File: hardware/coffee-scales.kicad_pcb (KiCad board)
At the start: 2 copper layers, 121.9 x 50.8 mm, 34 parts, among them J2 Conn_01x05, J3 AVR-ISP-6, Q1 MMBT4403, SW1 SW_Push, SW2 SW_Push, U2 ATmega328P-A, U3 4DIGIT_7SEG, U4 4DIGIT_7SEG, Y1 8MHz

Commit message: Infinite schematic/PCB changes
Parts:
- removed C6: 10uF, Capacitor_SMD:C_1210_3225Metric
- removed C8: 10uF, Capacitor_SMD:C_0805_2012Metric
- removed REF** (x3): MountingHole_3.2mm_M3, MountingHole:MountingHole_3.2mm_M3
- removed U4: 4DIGIT_7SEG, CoffeeLib:4DIGIT_7SEG
- added C13: 100pF, Capacitor_SMD:C_0603_1608Metric, F.Cu at (125.1, 146.1)
- added C15: 100pF, Capacitor_SMD:C_0603_1608Metric, F.Cu at (74.3, 146.1)
- added C16: 100pF, Capacitor_SMD:C_0603_1608Metric, F.Cu at (74.3, 149.2)
- added C17: 100pF, Capacitor_SMD:C_0603_1608Metric, F.Cu at (125.1, 149.2)
- added C18: 0.1uF, Capacitor_SMD:C_0603_1608Metric, F.Cu at (120.0, 151.3)
- added C19: 0.1uF, Capacitor_SMD:C_0603_1608Metric, F.Cu at (69.2, 151.3)
- added R10: 10k, Resistor_SMD:R_0603_1608Metric, F.Cu at (123.2, 149.2)
- added R7: 10k, Resistor_SMD:R_0603_1608Metric, F.Cu at (123.2, 146.1)
- added R8: 10k, Resistor_SMD:R_0603_1608Metric, F.Cu at (72.4, 149.2)
- added R9: 10k, Resistor_SMD:R_0603_1608Metric, F.Cu at (72.4, 146.1)
- added U1: ~, Package_SO:SOP-20_7.5x12.8mm_P1.27mm, F.Cu at (62.2, 151.1)
- added U6: ~, CoffeeLib:7_segment, F.Cu at (119.4, 165.1)
- added U7: ~, CoffeeLib:7_segment, F.Cu at (68.6, 165.1)
- U3: value 4DIGIT_7SEG -> ~; footprint CoffeeLib:4DIGIT_7SEG -> Package_SO:SOP-20_7.5x12.8mm_P1.27mm
- moved U3 56.6 mm to (113.0, 151.1)
- moved R6 18.5 mm to (50.6, 141.6)
- moved D1 18.2 mm to (47.0, 141.6)
- moved C3 5.96 mm to (152.4, 134.6), turned to 0 degrees
- moved C7 5.90 mm to (151.8, 138.4), turned to 0 degrees
- moved R5 5.08 mm to (59.1, 131.3)
- moved SW2 4.45 mm to (54.8, 131.3)
- moved C11 3.81 mm to (50.8, 131.3)
- moved C10 3.29 mm to (69.2, 129.5), turned to 180 degrees
- moved C5 3.27 mm to (119.4, 137.3)
- moved SW1 1.27 mm to (87.7, 162.6)
- moved C12 1.17 mm to (126.2, 138.4), turned to 180 degrees
- moved C9 1.10 mm to (72.2, 127.6), turned to 180 degrees
- moved L1 0.21 mm to (135.3, 138.4)
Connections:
- C12 pad 1: +3V3 -> VCC
- C5 pad 1: +3V3 -> VCC
- Q1 pad 2: +3V3 -> VCC
- U3 pad 1: unconnected-(U3-CLK-Pad1) -> GND
- U3 pad 2: unconnected-(U3-DIO-Pad2) -> Net-(U3-SEG1)
- U3 pad 3: GND -> Net-(U3-SEG2)
- U3 pad 4: +3V3 -> Net-(U3-SEG3)
- U3 pad 5: /328P/GPIO2 -> Net-(U3-SEG4)
- U3 pad 6: /328P/GPIO1 -> Net-(U3-SEG5)
- U3 pad 7: GND -> Net-(U3-SEG6)
- U3 pad 8: unconnected-(U3-5V-Pad8) -> Net-(U3-SEG7)
- U5 pad 1: +3V3 -> VCC
- U5 pad 16: +3V3 -> VCC
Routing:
- net VCC: track 69.5 -> 216.9 mm, vias 2 -> 8
- net +3V3: track 132.9 -> 0.00 mm, vias 1 -> 0
- net Net-(U3-SEG3): track 0.00 -> 38.6 mm
- net Net-(U1-SEG3): track 0.00 -> 38.6 mm
- net Net-(U1-SEG4): track 0.00 -> 30.8 mm
- net Net-(U3-SEG4): track 0.00 -> 30.8 mm
- net /328P/GPIO3: track 37.4 -> 8.62 mm
- net Net-(U1-SEG7): track 0.00 -> 28.0 mm
- net Net-(U3-SEG7): track 0.00 -> 28.0 mm
- net /328P/GPIO4: track 36.6 -> 9.43 mm
- net Net-(U1-SEG2): track 0.00 -> 25.3 mm
- net Net-(U3-SEG2): track 0.00 -> 25.3 mm
- net Net-(U3-SEG5): track 0.00 -> 23.2 mm
- net Net-(U1-SEG5): track 0.00 -> 23.2 mm
- net Net-(U1-SEG8): track 0.00 -> 22.4 mm
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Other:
- board text added: "A+ (Green)"
- board text added: "A- (White)"
- board text added: "Decoupling"
- board text added: "E+ (Red)"
- board text added: "E- (Black)"
- board text added: "Reset stuff"
- board text added: "SHLD (Yellow)"
- board text removed: "Black"
- board text removed: "Green"
- board text removed: "Red"
- board text removed: "Scale display"
- board text removed: "Shield"
- board text removed: "Timer display"
- board text removed: "White"

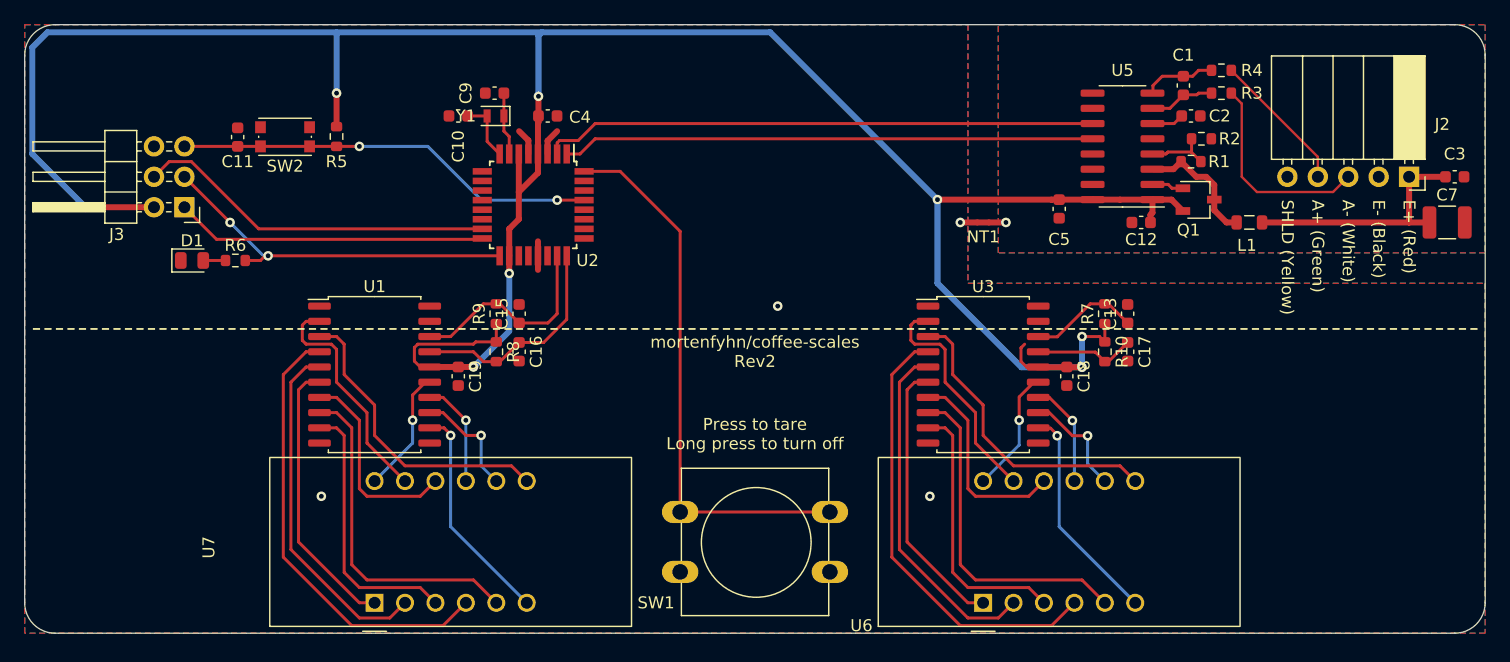
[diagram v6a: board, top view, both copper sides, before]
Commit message: Everything routed and checked, except power supply
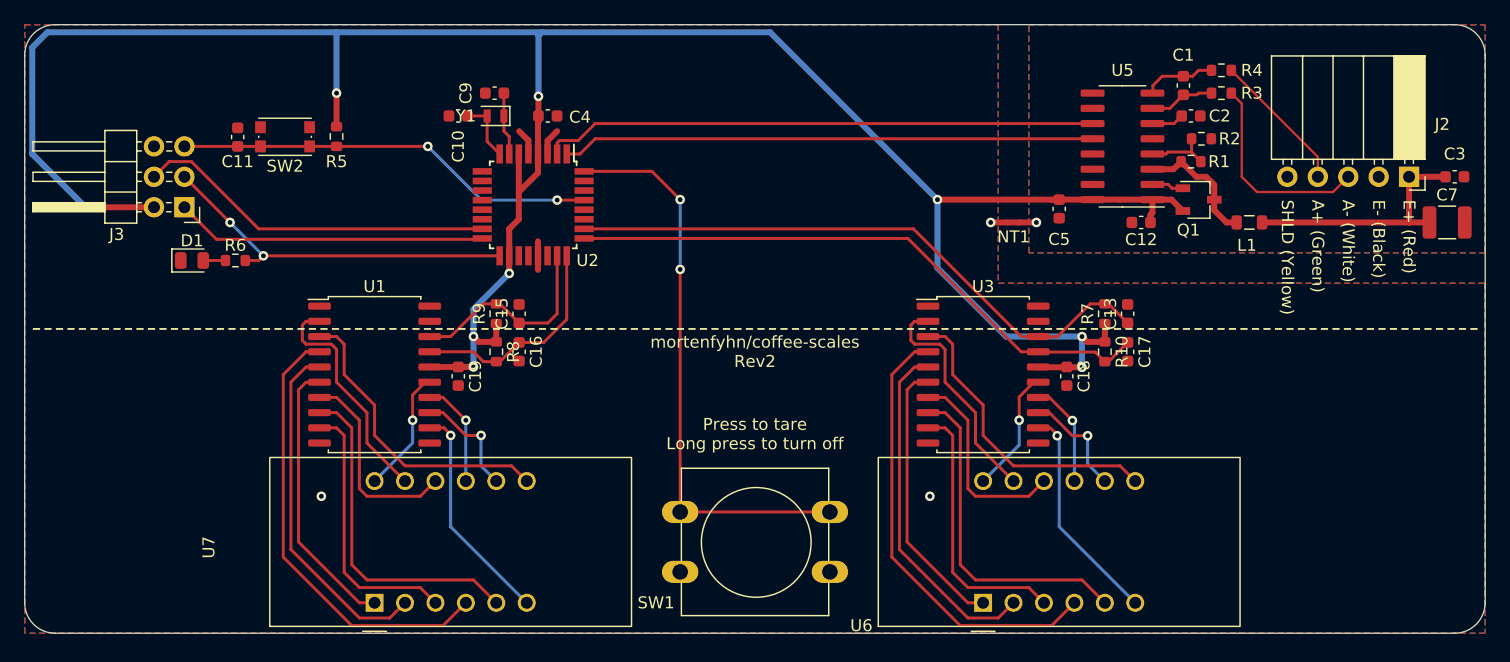
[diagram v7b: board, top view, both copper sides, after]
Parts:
- moved NT1 2.54 mm to (115.6, 138.4)
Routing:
- net /328P/GPIO3: track 8.62 -> 50.5 mm
- net /328P/GPIO4: track 9.43 -> 51.1 mm
- net VCC: track 216.9 -> 205.3 mm, vias 8 -> 9
- net /328P/INT0: track 46.0 -> 47.6 mm, vias 0 -> 2
- net GND: vias 4 -> 3

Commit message: Keep hacking
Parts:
- removed the C10 at (69.2, 129.5)
- removed the C9 at (72.2, 127.6)
- removed Y1: 8MHz, Crystal:Crystal_SMD_2012-2Pin_2.0x1.2mm
- added TP1: TestPoint, TestPoint:TestPoint_THTPad_D1.0mm_Drill0.5mm, F.Cu at (113.0, 138.4)
- added TP2: TestPoint, TestPoint:TestPoint_THTPad_D1.0mm_Drill0.5mm, F.Cu at (118.1, 138.4)
- added Y2: Resonator, Crystal:Resonator_SMD_Murata_CSTxExxV-3Pin_3.0x1.1mm, F.Cu at (71.8, 130.2)
- U3: renamed from U1; footprint Package_SO:SOP-20_7.5x12.8mm_P1.27mm -> CoffeeLib:SOP-20_7.5x12.8mm_P1.27mm_3d
- U5: renamed from U3; footprint Package_SO:SOP-20_7.5x12.8mm_P1.27mm -> CoffeeLib:SOP-20_7.5x12.8mm_P1.27mm_3d
- moved C8 0.64 mm to (120.0, 137.3)
- turned U4 to 0 degrees
- turned U6 to 0 degrees
- renumbered C11 to C1, C7 to C10, C15 to C11, C16 to C12, C19 to C13, C17 to C14, C13 to C15, C18 to C16, C12 to C5, C2 to C6, C1 to C7, C5 to C8, C3 to C9, J3 to J1, R5 to R1, R3 to R2, R4 to R3, R1 to R4, R2 to R5, R9 to R7, R7 to R9, SW2 to SW1, SW1 to SW2, U2 to U1, U5 to U2, U7 to U4
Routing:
- net /328P/XTAL1: track 5.26 -> 2.75 mm
- net /328P/XTAL2: track 5.24 -> 3.58 mm
- net HX_GNDA: track 1.41 -> 2.04 mm, vias 1 -> 3
- net GND: track 8.46 -> 9.10 mm, vias 3 -> 2
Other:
- board text added: "·Press to turn on ·Press to tare ·Long press to turn off"
- board text removed: "Press to tare Long press to turn off"
